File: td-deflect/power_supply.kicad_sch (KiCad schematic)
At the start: 28 parts, among them J1 Conn_01x08_Socket, J1 Conn_01x12_Socket, J17 Barrel_Jack, J18 Conn_01x02_Male, J3 Conn_01x04_Male

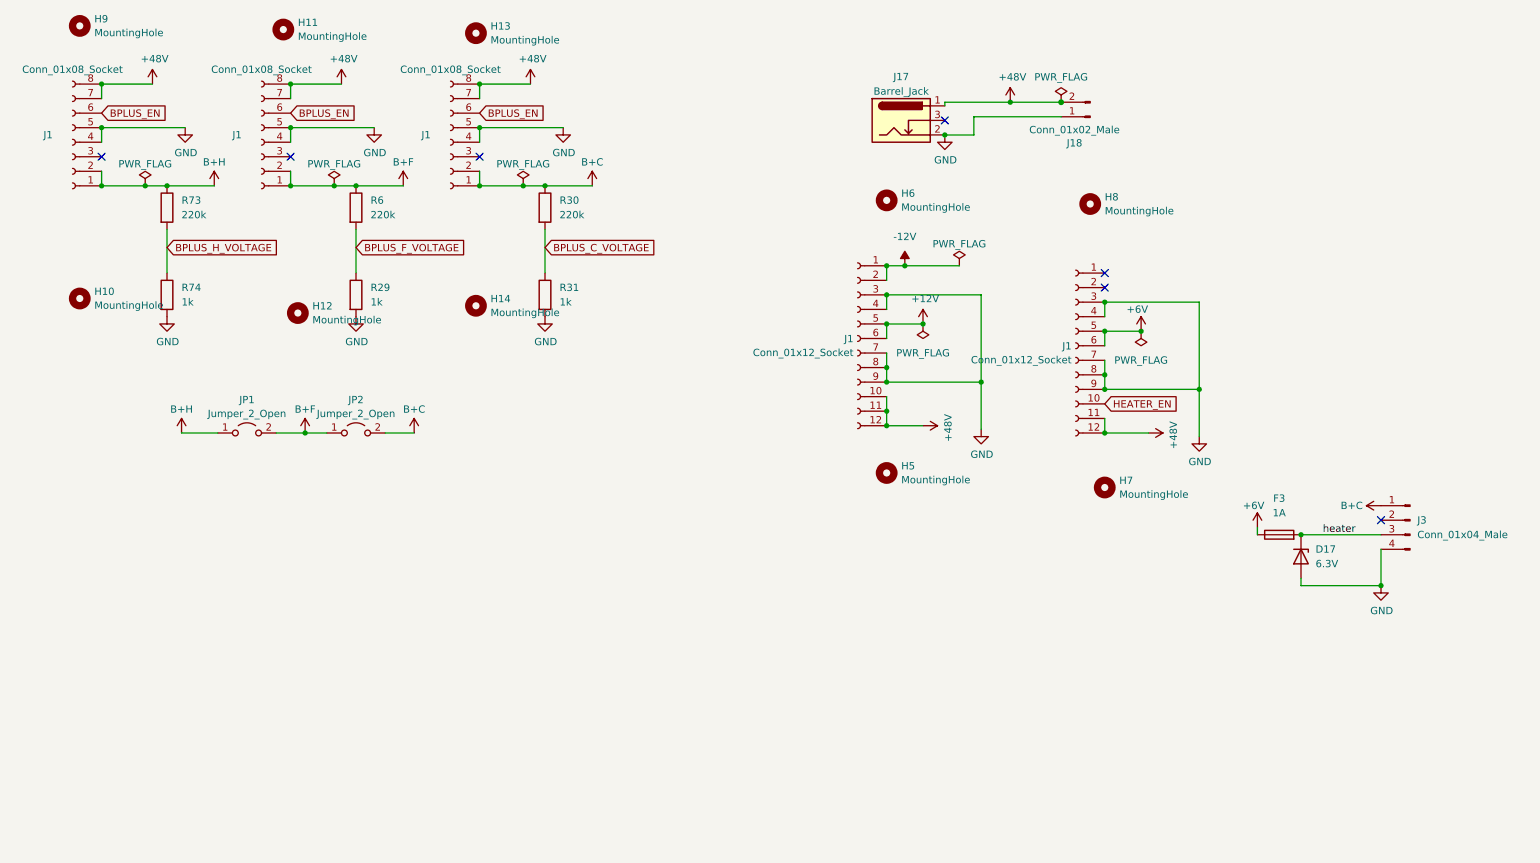
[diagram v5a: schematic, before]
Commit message: update td-deflect kicad version
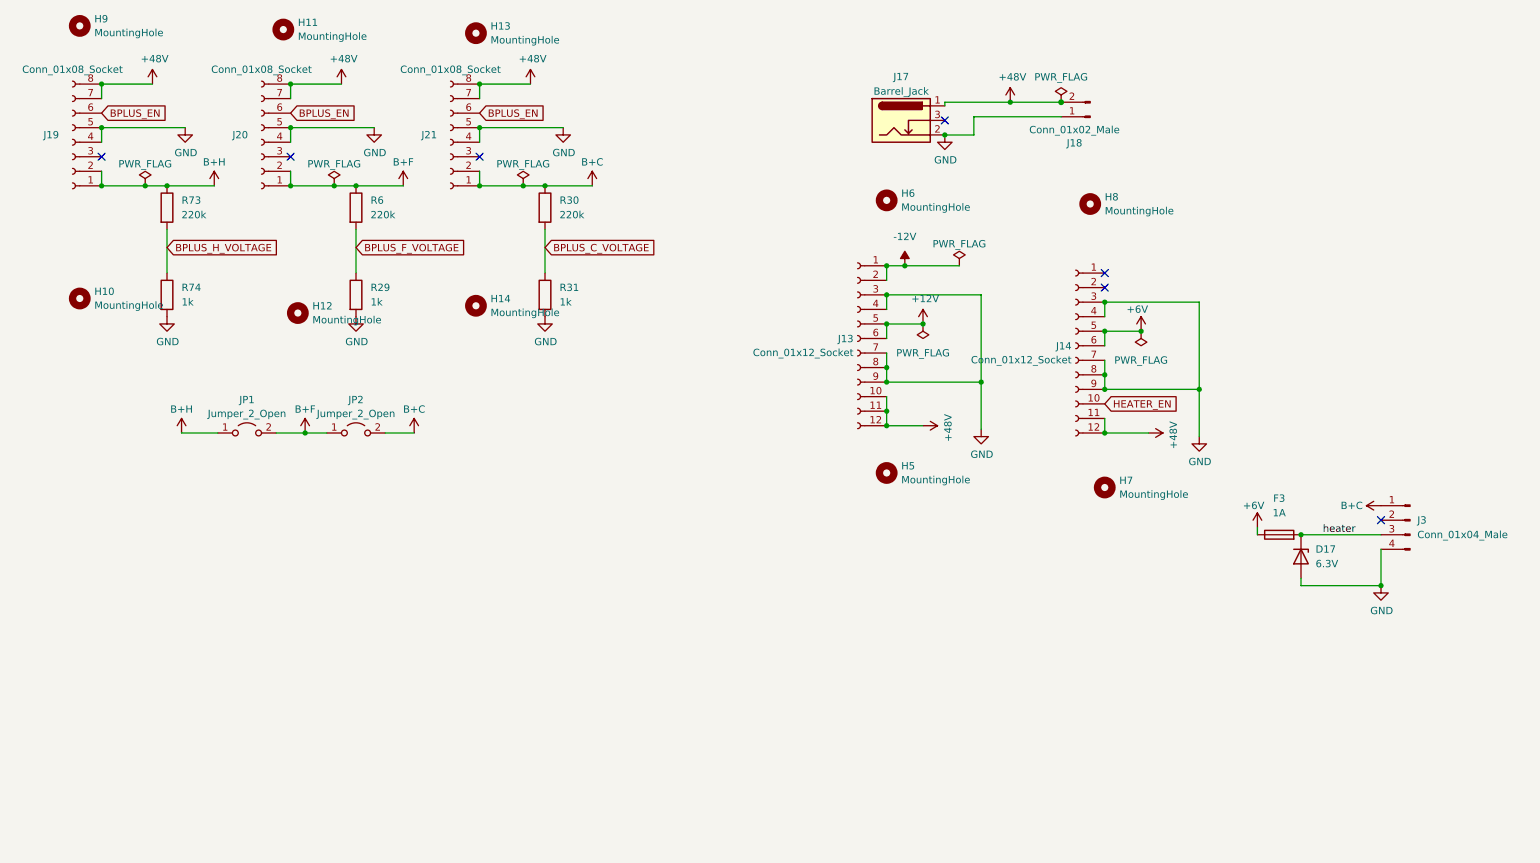
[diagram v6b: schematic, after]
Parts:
- renumbered J1 to J13, J1 to J14, J1 to J19, J1 to J20, J1 to J21

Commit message: shrink board a lot
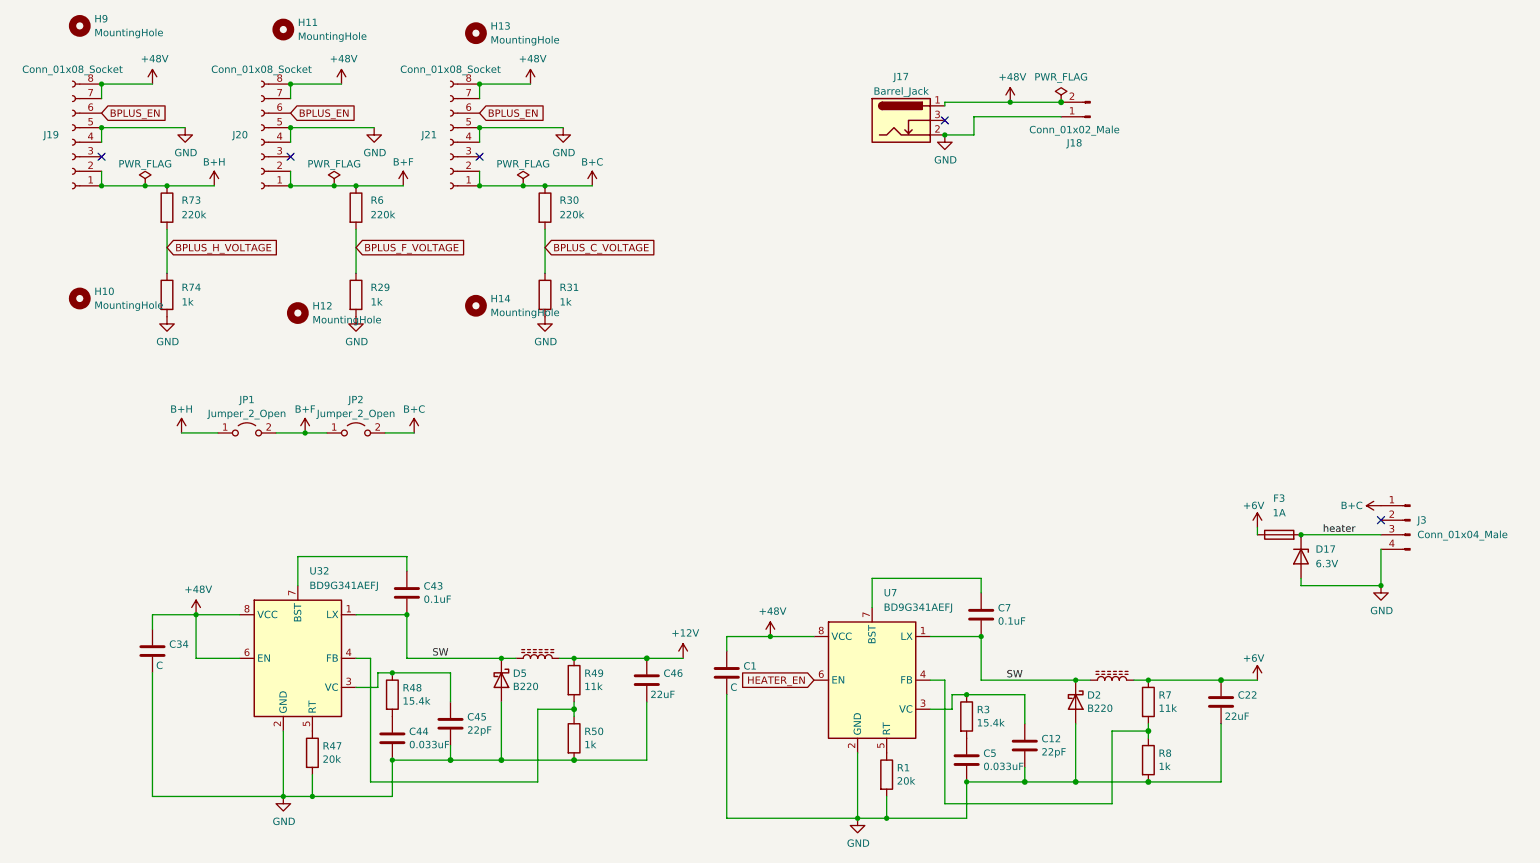
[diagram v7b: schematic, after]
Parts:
- removed H5, H6, H7, H8: MountingHole, MountingHole:MountingHole_3.2mm_M3, symbol Mechanical:MountingHole
- removed J13, J14: Conn_01x12_Socket, Connector_PinSocket_2.54mm:PinSocket_1x12_P2.54mm_Vertical, symbol Connector:Conn_01x12_Socket
- added C1, C34: C, Capacitor_SMD:C_1210_3225Metric, symbol Device:C
- added C12, C45: 22pF, Capacitor_SMD:C_0805_2012Metric, symbol Device:C
- added C22, C46: 22uF, Capacitor_SMD:C_0805_2012Metric, symbol Device:C
- added C43, C7: 0.1uF, Capacitor_SMD:C_0805_2012Metric, symbol Device:C
- added C44, C5: 0.033uF, Capacitor_SMD:C_0805_2012Metric, symbol Device:C
- added D2, D5: B220, Diode_SMD:D_SMB, symbol Diode:B220
- added L1, L5: 47uH, Inductor_SMD:L_Bourns_SRR1260, symbol Device:L_Ferrite
- added R1, R47: 20k, Resistor_SMD:R_0805_2012Metric, symbol Device:R
- added R3, R48: 15.4k, Resistor_SMD:R_0805_2012Metric, symbol Device:R
- added R49, R7: 11k, Resistor_SMD:R_0805_2012Metric, symbol Device:R
- added R50, R8: 1k, Resistor_SMD:R_0805_2012Metric, symbol Device:R
- added U32, U7: BD9G341AEFJ, Package_SO:SOIC-8-1EP_3.9x4.9mm_P1.27mm_EP2.41x3.3mm_ThermalVias, symbol Regulator_Switching:BD9G341EFJ
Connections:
- net +12V: now also C46.1, L5.2, R49.1
- net +48V: now also C1.1, C34.1, U32.6 (EN), U32.8 (VCC), U7.8 (VCC)
- net +6V: now also C22.1, L1.2, R7.1
- net GND: now also C1.2, C12.2, C22.2, C34.2, C44.2, C45.2, C46.2, C5.2, D2.2 (A), D5.2 (A), R1.2, R47.2, R50.2, R8.2, U32.2 (GND), U32.9 (GND), U7.2 (GND), U7.9 (GND)
- net HEATER_EN: now also U7.6 (EN)
- new net: R47.1, U32.5 (RT)
- new net: C44.1, R48.2
- new net: C45.1, R48.1, U32.3 (VC)
- new net: C43.1, U32.7 (BST)
- new net: R49.2, R50.1, U32.4 (FB)
- new net: C7.1, U7.7 (BST)
- new net: C12.1, R3.1, U7.3 (VC)
- new net: C5.1, R3.2
- new net: R1.1, U7.5 (RT)
- new net: R7.2, R8.1, U7.4 (FB)
- new net SW: C43.2, C7.2, D2.1 (K), D5.1 (K), L1.1, L5.1, U32.1 (LX), U7.1 (LX)
- no-connect marks 7 -> 5

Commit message: finish board
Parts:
- added C27: 0.1uF, Capacitor_SMD:C_0805_2012Metric, symbol Device:C
- added R11, R9: 1k, Resistor_SMD:R_0805_2012Metric, symbol Device:R
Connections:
- net GND: now also C27.2, R11.2
- net SW renamed SW_12V
- net SW_12V: no longer C43.2, D5.1 (K), L5.1, U32.1 (LX)
- new net +3.3VA: R9.1
- new net SW_48V: C43.2, D5.1 (K), L5.1, U32.1 (LX)
- new net virtual_ground: C27.1, R11.1, R9.2
